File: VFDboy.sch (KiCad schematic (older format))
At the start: 37 parts, among them J1 AVR-ISP-6, SW1 RIGHT, SW2 A, SW3 DOWN, SW4 UP, SW5 LEFT, SW6 B, U1 ATmega32U4-MU, U2 SSD1306_VFD, U7 SRV05-4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

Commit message: Finish layout
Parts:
- D1, D2: footprint Diode_SMD:D_0603_1608Metric -> LED_SMD:LED_0603_1608Metric
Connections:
- net +5V: now also D1.2 (A), D2.2 (A); no longer R5.1, R6.1
- net at U1.22 (PD5): now also R6.2; no longer D2.1 (K)
- net at U1.8 (PB0): now also R5.2; no longer D1.1 (K)
- new net: D2.1 (K), R6.1
- new net: D1.1 (K), R5.1
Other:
- moved on the sheet: D1, D2, R5, R6
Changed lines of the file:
@@
 L Device:LED D2
 U 1 1 600270E6
-P 7150 3850
-F 0 "D2" H 7143 4067 50  0000 C CNN
-F 1 "YLW" H 7143 3976 50  0000 C CNN
-F 2 "Diode_SMD:D_0603_1608Metric" H 7150 3850 50  0001 C CNN
-F 3 "~" H 7150 3850 50  0001 C CNN
-F 4 "C72038" H 7150 3850 50  0001 C CNN "LCSC"
-	1    7150 3850
+P 7650 3850
+F 0 "D2" H 7643 4067 50  0000 C CNN
+F 1 "YLW" H 7643 3976 50  0000 C CNN
+F 2 "LED_SMD:LED_0603_1608Metric" H 7650 3850 50  0001 C CNN
+F 3 "~" H 7650 3850 50  0001 C CNN
+F 4 "C72038" H 7650 3850 50  0001 C CNN "LCSC"
+	1    7650 3850
 	1    0    0    -1
 $EndComp
@@
 L Device:R R6
 U 1 1 60027C4F
-P 7650 3850
-F 0 "R6" V 7443 3850 50  0000 C CNN
-F 1 "3.3kR" V 7534 3850 50  0000 C CNN
-F 2 "Resistor_SMD:R_0402_1005Metric" V 7580 3850 50  0001 C CNN
-F 3 "~" H 7650 3850 50  0001 C CNN
-F 4 "C25890" V 7650 3850 50  0001 C CNN "LCSC"
-	1    7650 3850
+P 7150 3850
+F 0 "R6" V 6943 3850 50  0000 C CNN
+F 1 "3.3kR" V 7034 3850 50  0000 C CNN
+F 2 "Resistor_SMD:R_0402_1005Metric" V 7080 3850 50  0001 C CNN
+F 3 "~" H 7150 3850 50  0001 C CNN
+F 4 "C25890" V 7150 3850 50  0001 C CNN "LCSC"
+	1    7150 3850
 	0    1    1    0
 $EndComp
@@
 L Device:LED D1
 U 1 1 6003B6D5
-P 7150 1700
-F 0 "D1" H 7143 1917 50  0000 C CNN
-F 1 "GRN" H 7143 1826 50  0000 C CNN
-F 2 "Diode_SMD:D_0603_1608Metric" H 7150 1700 50  0001 C CNN
-F 3 "~" H 7150 1700 50  0001 C CNN
-F 4 "C72043" H 7150 1700 50  0001 C CNN "LCSC"
-	1    7150 1700
+P 7650 1700
+F 0 "D1" H 7643 1917 50  0000 C CNN
+F 1 "GRN" H 7643 1826 50  0000 C CNN
+F 2 "LED_SMD:LED_0603_1608Metric" H 7650 1700 50  0001 C CNN
+F 3 "~" H 7650 1700 50  0001 C CNN
+F 4 "C72043" H 7650 1700 50  0001 C CNN "LCSC"
+	1    7650 1700
 	1    0    0    -1
 $EndComp
@@
 L Device:R R5
 U 1 1 600450CC
-P 7650 1700
-F 0 "R5" V 7443 1700 50  0000 C CNN
-F 1 "8.2kR" V 7534 1700 50  0000 C CNN
-F 2 "Resistor_SMD:R_0402_1005Metric" V 7580 1700 50  0001 C CNN
-F 3 "~" H 7650 1700 50  0001 C CNN
-F 4 "C25924" V 7650 1700 50  0001 C CNN "LCSC"
-	1    7650 1700
+P 7150 1700
+F 0 "R5" V 6943 1700 50  0000 C CNN
+F 1 "8.2kR" V 7034 1700 50  0000 C CNN
+F 2 "Resistor_SMD:R_0402_1005Metric" V 7080 1700 50  0001 C CNN
+F 3 "~" H 7150 1700 50  0001 C CNN
+F 4 "C25924" V 7150 1700 50  0001 C CNN "LCSC"
+	1    7150 1700
 	0    1    1    0
 $EndComp

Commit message: Add additional mounting holes
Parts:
- added H4, H5, H6, H7, H8, H9: MountingHole, MountingHole:MountingHole_3.2mm_M3, symbol Mechanical:MountingHole
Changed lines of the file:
@@
 Wire Wire Line
 	550  5600 800  5600
+$Comp
+L Mechanical:MountingHole H6
+U 1 1 61838AD4
+P 4550 7550
+F 0 "H6" H 4650 7596 50  0000 L CNN
+F 1 "MountingHole" H 4650 7505 50  0000 L CNN
+F 2 "MountingHole:MountingHole_3.2mm_M3" H 4550 7550 50  0001 C CNN
+F 3 "~" H 4550 7550 50  0001 C CNN
+	1    4550 7550
+	1    0    0    -1
+$EndComp
+$Comp
+L Mechanical:MountingHole H5
+U 1 1 61839028
+P 4550 7350
+F 0 "H5" H 4650 7396 50  0000 L CNN
+F 1 "MountingHole" H 4650 7305 50  0000 L CNN
+F 2 "MountingHole:MountingHole_3.2mm_M3" H 4550 7350 50  0001 C CNN
+F 3 "~" H 4550 7350 50  0001 C CNN
+	1    4550 7350
+	1    0    0    -1
+$EndComp
+$Comp
+L Mechanical:MountingHole H4
+U 1 1 618434E7
+P 4550 7150
+F 0 "H4" H 4650 7196 50  0000 L CNN
+F 1 "MountingHole" H 4650 7105 50  0000 L CNN
+F 2 "MountingHole:MountingHole_3.2mm_M3" H 4550 7150 50  0001 C CNN
+F 3 "~" H 4550 7150 50  0001 C CNN
+	1    4550 7150
+	1    0    0    -1
+$EndComp
+$Comp
+L Mechanical:MountingHole H9
+U 1 1 6184DCD9
+P 5300 7550
+F 0 "H9" H 5400 7596 50  0000 L CNN
+F 1 "MountingHole" H 5400 7505 50  0000 L CNN
+F 2 "MountingHole:MountingHole_3.2mm_M3" H 5300 7550 50  0001 C CNN
+F 3 "~" H 5300 7550 50  0001 C CNN
+	1    5300 7550
+	1    0    0    -1
+$EndComp
+$Comp
+L Mechanical:MountingHole H8
+U 1 1 6184DCDF
+P 5300 7350
+F 0 "H8" H 5400 7396 50  0000 L CNN
+F 1 "MountingHole" H 5400 7305 50  0000 L CNN
+F 2 "MountingHole:MountingHole_3.2mm_M3" H 5300 7350 50  0001 C CNN
+F 3 "~" H 5300 7350 50  0001 C CNN
+	1    5300 7350
+	1    0    0    -1
+$EndComp
+$Comp
+L Mechanical:MountingHole H7
+U 1 1 6184DCE5
+P 5300 7150
+F 0 "H7" H 5400 7196 50  0000 L CNN
+F 1 "MountingHole" H 5400 7105 50  0000 L CNN
+F 2 "MountingHole:MountingHole_3.2mm_M3" H 5300 7150 50  0001 C CNN
+F 3 "~" H 5300 7150 50  0001 C CNN
+	1    5300 7150
+	1    0    0    -1
+$EndComp
 $EndSCHEMATC

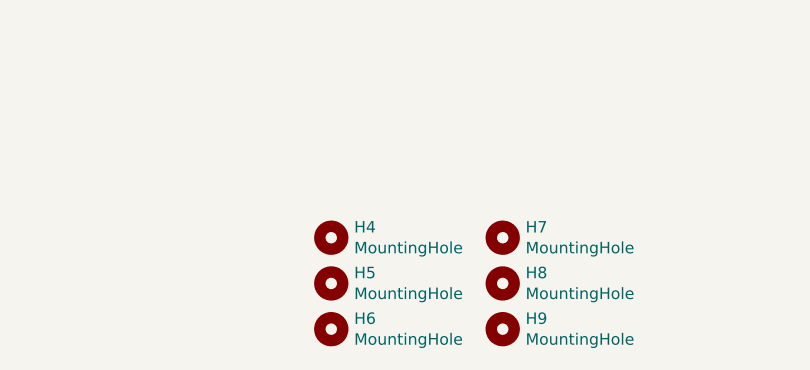
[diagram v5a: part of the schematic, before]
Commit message: Route SD interface
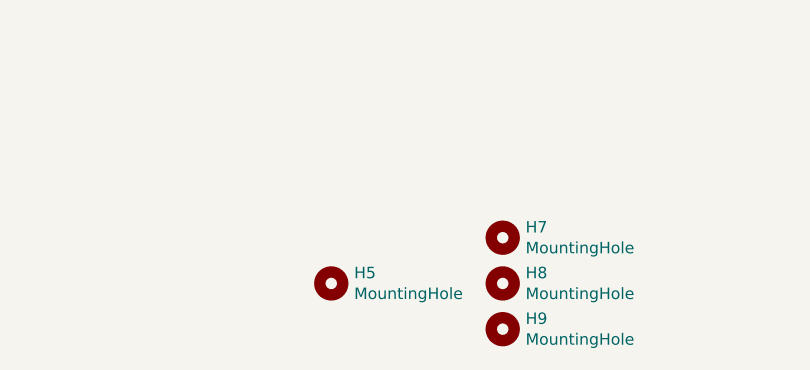
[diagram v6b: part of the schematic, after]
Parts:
- removed H4, H6: MountingHole, MountingHole:MountingHole_3.2mm_M3, symbol Mechanical:MountingHole
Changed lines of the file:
@@
 	550  5600 800  5600
-$Comp
-L Mechanical:MountingHole H6
-U 1 1 61838AD4
-P 4550 7550
-F 0 "H6" H 4650 7596 50  0000 L CNN
-F 1 "MountingHole" H 4650 7505 50  0000 L CNN
-F 2 "MountingHole:MountingHole_3.2mm_M3" H 4550 7550 50  0001 C CNN
-F 3 "~" H 4550 7550 50  0001 C CNN
-	1    4550 7550
-	1    0    0    -1
-$EndComp
 $Comp
 L Mechanical:MountingHole H5
@@
 	1    0    0    -1
 $EndComp
-$Comp
-L Mechanical:MountingHole H4
-U 1 1 618434E7
-P 4550 7150
-F 0 "H4" H 4650 7196 50  0000 L CNN
-F 1 "MountingHole" H 4650 7105 50  0000 L CNN
-F 2 "MountingHole:MountingHole_3.2mm_M3" H 4550 7150 50  0001 C CNN
-F 3 "~" H 4550 7150 50  0001 C CNN
-	1    4550 7150
-	1    0    0    -1
-$EndComp

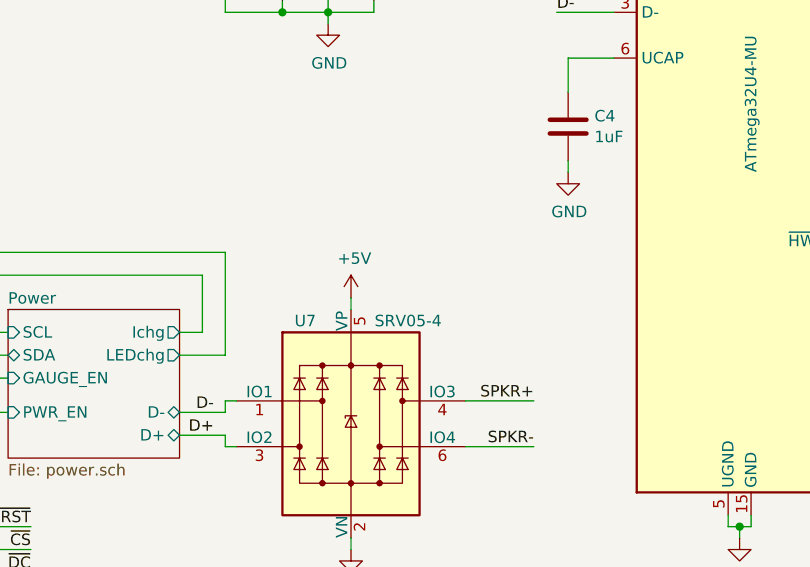
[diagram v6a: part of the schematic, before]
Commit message: Connect buttons
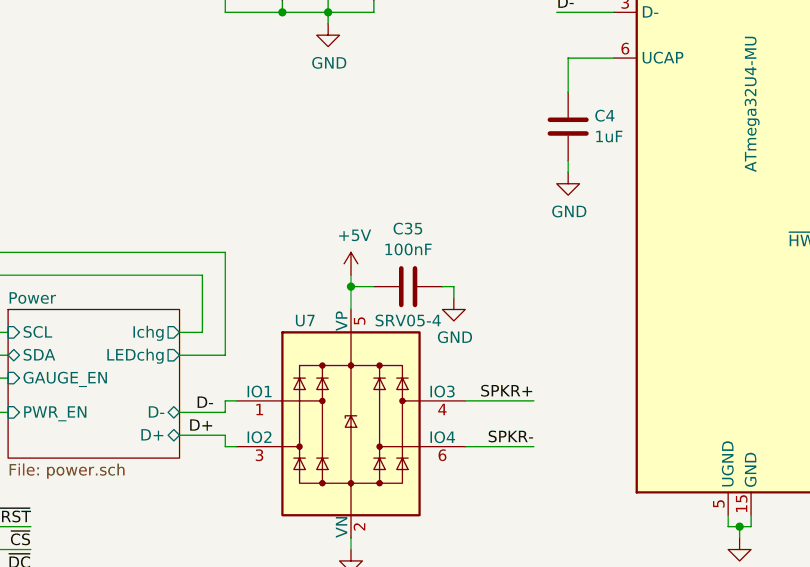
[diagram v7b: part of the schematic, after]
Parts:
- added C35: 100nF, Capacitor_SMD:C_0402_1005Metric, symbol Device:C
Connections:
- net +5V: now also C35.1
- net GND: now also C35.2
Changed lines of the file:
@@
 	1    0    0    -1
 $EndComp
-Wire Wire Line
-	3550 4500 3550 4550
 $Comp
 L power:GND #PWR0101
@@
 L power:+5V #PWR0102
 U 1 1 6087AF0F
-P 3550 4500
-F 0 "#PWR0102" H 3550 4350 50  0001 C CNN
-F 1 "+5V" H 3565 4673 50  0000 C CNN
-F 2 "" H 3550 4500 50  0001 C CNN
-F 3 "" H 3550 4500 50  0001 C CNN
-	1    3550 4500
+P 3550 4400
+F 0 "#PWR0102" H 3550 4250 50  0001 C CNN
+F 1 "+5V" H 3565 4573 50  0000 C CNN
+F 2 "" H 3550 4400 50  0001 C CNN
+F 3 "" H 3550 4400 50  0001 C CNN
+	1    3550 4400
 	1    0    0    -1
 $EndComp
@@
 	1    0    0    -1
 $EndComp
+$Comp
+L Device:C C35
+U 1 1 61D5B828
+P 3800 4450
+F 0 "C35" V 4052 4450 50  0000 C CNN
+F 1 "100nF" V 3961 4450 50  0000 C CNN
+F 2 "Capacitor_SMD:C_0402_1005Metric" H 3838 4300 50  0001 C CNN
+F 3 "~" H 3800 4450 50  0001 C CNN
+F 4 "C1525" H 3800 4450 50  0001 C CNN "LCSC"
+	1    3800 4450
+	0    -1   -1   0
+$EndComp
+Wire Wire Line
+	3550 4400 3550 4450
+Wire Wire Line
+	3650 4450 3550 4450
+Connection ~ 3550 4450
+Wire Wire Line
+	3550 4450 3550 4550
+$Comp
+L power:GND #PWR0133
+U 1 1 61D7B83D
+P 4000 4500
+F 0 "#PWR0133" H 4000 4250 50  0001 C CNN
+F 1 "GND" H 4005 4327 50  0000 C CNN
+F 2 "" H 4000 4500 50  0001 C CNN
+F 3 "" H 4000 4500 50  0001 C CNN
+	1    4000 4500
+	1    0    0    -1
+$EndComp
+Wire Wire Line
+	4000 4500 4000 4450
+Wire Wire Line
+	4000 4450 3950 4450
 $EndSCHEMATC

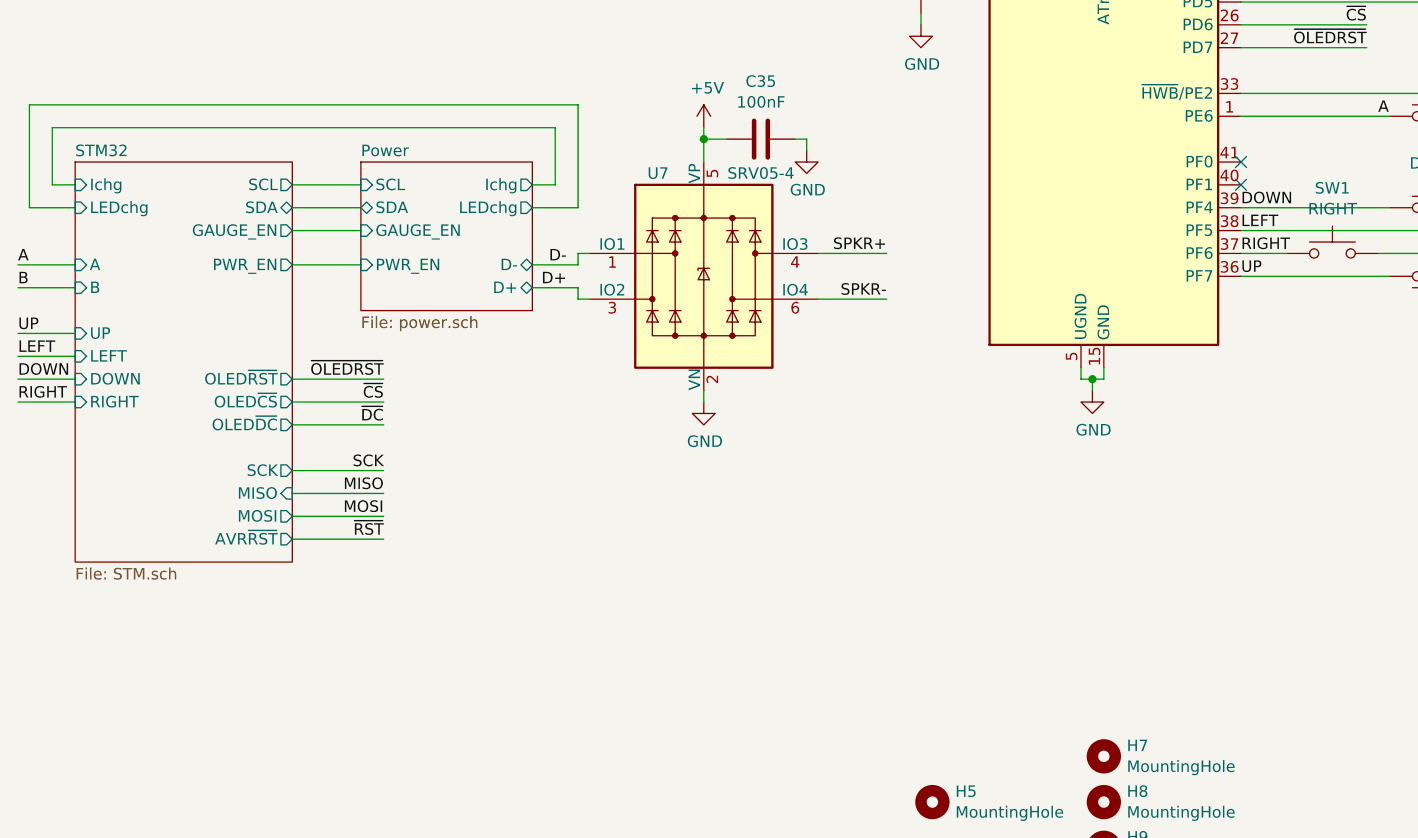
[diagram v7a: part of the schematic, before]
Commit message: Add support for GBA D-Pad mounting
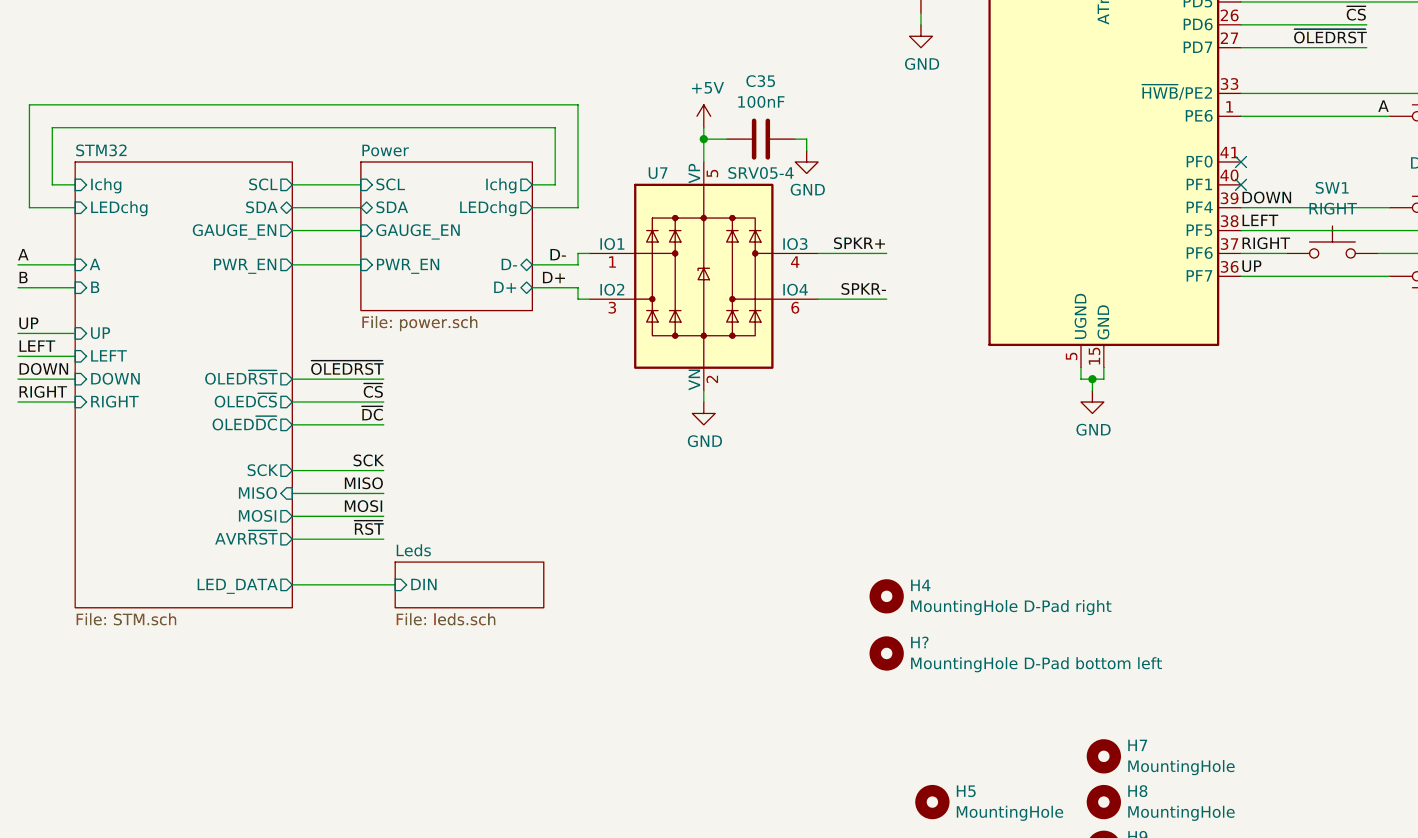
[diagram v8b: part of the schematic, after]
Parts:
- added H4: MountingHole D-Pad right, MountingHole_GBA:MountingHole_GBA_DPAD, symbol Mechanical:MountingHole
- added H?: MountingHole D-Pad bottom left, MountingHole_GBA:MountingHole_GBA_DPAD, symbol Mechanical:MountingHole
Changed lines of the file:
@@
 $Descr A4 11693 8268
 encoding utf-8
-Sheet 1 4
+Sheet 1 23
 Title ""
 Date ""
@@
 MISO
 $Sheet
-S 800  4550 950  1750
+S 800  4550 950  1950
 U 60CF39C0
 F0 "STM32" 50
@@
 F19 "DOWN" I L 800 5500 50
 F20 "RIGHT" I L 800 5600 50
+F21 "LED_DATA" O R 1750 6400 50
 $EndSheet
 Text Label 2150 5500 2    50   ~ 0
@@
 Wire Wire Line
 	4000 4450 3950 4450
+$Sheet
+S 2200 6300 650  200
+U 62050786
+F0 "Leds" 50
+F1 "leds.sch" 50
+F2 "DIN" I L 2200 6400 50
+$EndSheet
+Wire Wire Line
+	2200 6400 1750 6400
+$Comp
+L Mechanical:MountingHole H4
+U 1 1 620E044D
+P 4350 6450
+F 0 "H4" H 4450 6496 50  0000 L CNN
+F 1 "MountingHole D-Pad right" H 4450 6405 50  0000 L CNN
+F 2 "MountingHole_GBA:MountingHole_GBA_DPAD" H 4350 6450 50  0001 C CNN
+F 3 "~" H 4350 6450 50  0001 C CNN
+	1    4350 6450
+	1    0    0    -1
+$EndComp
+$Comp
+L Mechanical:MountingHole H?
+U 1 1 620E34B6
+P 4350 6700
+F 0 "H?" H 4450 6746 50  0000 L CNN
+F 1 "MountingHole D-Pad bottom left" H 4450 6655 50  0000 L CNN
+F 2 "MountingHole_GBA:MountingHole_GBA_DPAD" H 4350 6700 50  0001 C CNN
+F 3 "~" H 4350 6700 50  0001 C CNN
+	1    4350 6700
+	1    0    0    -1
+$EndComp
 $EndSCHEMATC
